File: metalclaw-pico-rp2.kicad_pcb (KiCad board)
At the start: 4 copper layers, 21 x 51 mm, 123 parts, among them J1 USB4105-GF-A, J2 FTSH-105-01-L-DV-K, SW1 PTS810SJM250SMTR LFS, SW2 PTS810SJM250SMTR LFS, U1 XC6220B331MR-G, U2 RP2354B, U3 APS6404L-3SQR-SN, Y1 ABM8-272-T3

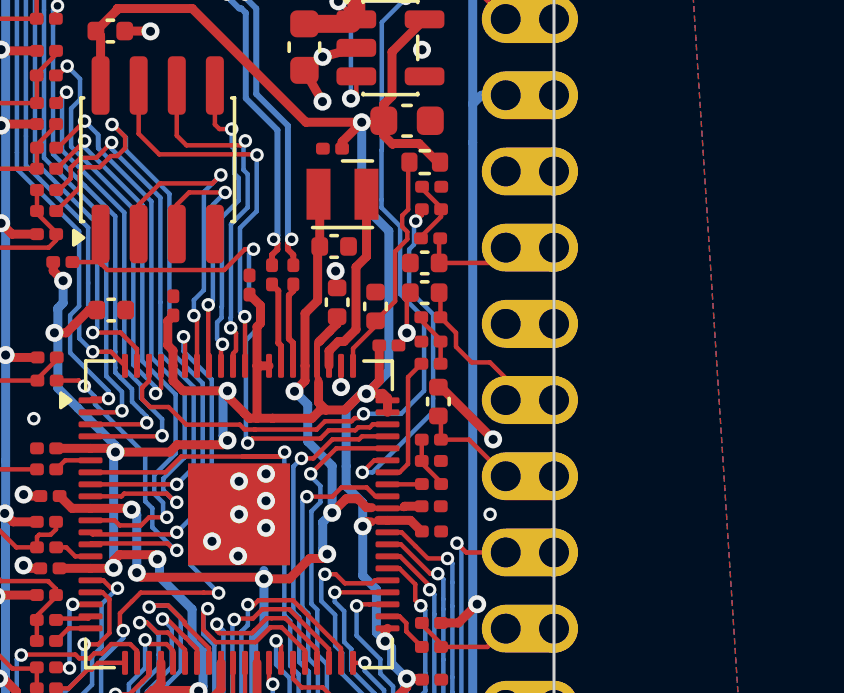
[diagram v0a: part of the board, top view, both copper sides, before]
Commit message: Add GND return vias for C29 and C9 decoupling loops
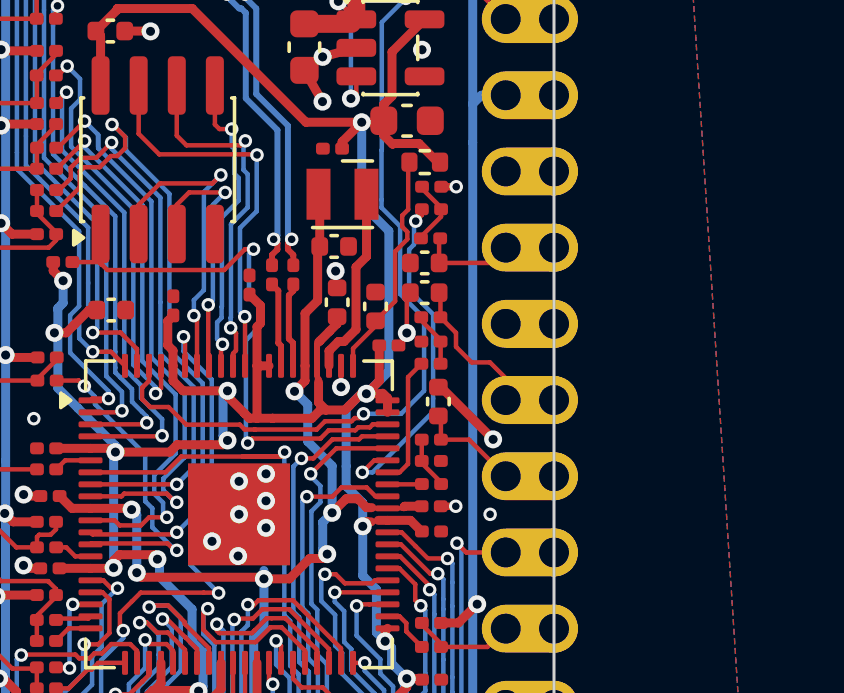
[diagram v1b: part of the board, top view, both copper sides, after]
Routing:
- net GND: track 23.9 -> 24.9 mm, vias 29 -> 31
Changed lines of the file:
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@@
 			(size 0.65 0.65)
 			(drill 0.65)
-			(layers "*.Cu" "*.Mask")
+			(layers "F&B.Cu" "*.Mask")
 		)
 		(pad "" np_thru_hole circle
@@
 			(size 0.65 0.65)
 			(drill 0.65)
-			(layers "*.Cu" "*.Mask")
+			(layers "F&B.Cu" "*.Mask")
 		)
 		(pad "A1" smd roundrect
@@
 	)
 	(segment
+		(start 170.535 98.6)
+		(end 171.035 98.6)
+		(width 0.25)
+		(layer "F.Cu")
+		(net 4)
+	)
+	(segment
 		(start 167.72 83.32)
 		(end 166.597111 83.620877)
@@
 	)
 	(segment
+		(start 170.55 87.95)
+		(end 171.05 87.95)
+		(width 0.25)
+		(layer "F.Cu")
+		(net 4)
+	)
+	(segment
 		(start 161.17 81.12)
 		(end 160.464874 81.308937)
@@
 	)
 	(via
+		(at 171.035 98.6)
+		(size 0.45)
+		(drill 0.25)
+		(layers "F.Cu" "B.Cu")
+		(net 4)
+	)
+	(via
 		(at 156.97 95.68)
 		(size 0.45)
@@
 		(layers "F.Cu" "B.Cu")
 		(net 4)
+	)
+	(via
+		(at 171.05 87.95)
+		(size 0.45)
+		(drill 0.25)
+		(layers "F.Cu" "B.Cu")
+		(net 4)

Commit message: Ground some passives better
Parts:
- moved R23 0.17 mm to (170.2, 89.5)
- moved C5 0.14 mm to (170.0, 91.3), turned to 180 degrees
- moved C4 0.07 mm to (170.0, 90.4), turned to 180 degrees
- turned R32 to 180 degrees
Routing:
- net Net-(A1-GPIO28_ADC2): track 3.32 -> 4.64 mm
- net Net-(A1-GPIO27_ADC1): track 4.92 -> 5.83 mm
- net Net-(C9-Pad2): track 2.54 -> 1.67 mm
- net GND: track 24.9 -> 24.2 mm

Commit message: Fix DRC warnings
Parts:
- moved R23 0.09 mm to (170.2, 89.4)
- moved C4 0.08 mm to (170.0, 90.3)
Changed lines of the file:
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@@
 	(footprint "Resistor_SMD:R_0201_0603Metric"
 		(layer "F.Cu")
-		(at 170.195 89.5)
+		(at 170.19 89.41)
 		(descr "Resistor SMD 0201 (0603 Metric), square (rectangular) end terminal, IPC-7351 nominal, (Body size source: https://www.vishay.com/docs/20052/crcw0201e3.pdf), generated with kicad-footprint-generator")
 		(tags "resistor")
@@
 	(footprint "Capacitor_SMD:C_0402_1005Metric"
 		(layer "F.Cu")
-		(at 170 90.42 180)
+		(at 170 90.34 180)
 		(descr "Capacitor SMD 0402 (1005 Metric), square (rectangular) end terminal, IPC-7351 nominal, (Body size source: IPC-SM-782 page 76, https://www.pcb-3d.com/wordpress/wp-content/uploads/ipc-sm-782a_amendment_1_and_2.pdf), generated with kicad-footprint-generator")
 		(tags "capacitor")
@@
 	)
 	(segment
-		(start 169.52 90.43)
-		(end 169.648518 90.43)
+		(start 172.2 89.48)
+		(end 172.7 89.98)
 		(width 0.15)
 		(layer "F.Cu")
@@
 	)
 	(segment
-		(start 169.52 90.42)
-		(end 169.648518 90.42)
+		(start 169.52 90.43)
+		(end 169.648518 90.43)
 		(width 0.15)
 		(layer "F.Cu")
@@
 	)
 	(segment
-		(start 172.22 89.5)
-		(end 172.7 89.98)
+		(start 169.52 90.42)
+		(end 169.648518 90.42)
 		(width 0.15)
 		(layer "F.Cu")
@@
 	)
 	(segment
-		(start 170.515 89.5)
-		(end 172.22 89.5)
+		(start 169.648518 90.34)
+		(end 169.52 90.34)
 		(width 0.15)
 		(layer "F.Cu")
@@
 	)
 	(segment
-		(start 170.515 89.553518)
-		(end 170.515 89.5)
+		(start 170.51 89.478518)
+		(end 169.648518 90.34)
 		(width 0.15)
 		(layer "F.Cu")
@@
 	)
 	(segment
-		(start 169.648518 90.42)
-		(end 170.515 89.553518)
+		(start 172.19 90.49)
+		(end 172.7 89.98)
 		(width 0.15)
 		(layer "F.Cu")
@@
 	)
 	(segment
-		(start 172.19 90.49)
-		(end 172.7 89.98)
+		(start 170.515 89.48)
+		(end 172.2 89.48)
 		(width 0.15)
 		(layer "F.Cu")
@@
 	)
 	(segment
-		(start 169.19 89.884)
-		(end 169.014 90.06)
-		(width 0.15)
-		(layer "F.Cu")
-		(net 15)
-	)
-	(segment
 		(start 169.35 88.561196)
 		(end 169.454 88.457196)
@@
 	)
 	(segment
-		(start 169.014 90.06)
-		(end 169.014 91.766)
+		(start 169.35 89.6)
+		(end 169.35 88.561196)
 		(width 0.15)
 		(layer "F.Cu")
@@
 	)
 	(segment
-		(start 169.35 89.724)
-		(end 169.35 88.561196)
+		(start 169.014 89.936)
+		(end 169.35 89.6)
 		(width 0.15)
 		(layer "F.Cu")
@@
 	)
 	(segment
-		(start 169.014 90.06)
-		(end 169.35 89.724)
+		(start 169.014 91.766)
+		(end 169.014 89.936)
 		(width 0.15)
 		(layer "F.Cu")

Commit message: Use net tie to connect AGND and GND
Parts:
- added NT1: NetTie_2, NetTie:NetTie-2_SMD_Pad0.5mm, B.Cu at (171.4, 91.7)
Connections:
- A1 pad 33: GND -> Net-(A1-AGND)
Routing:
- net Net-(A1-AGND): track 0.00 -> 1.45 mm
- net +3.3VP: track 143.4 -> 144.2 mm
- net GND: track 24.2 -> 24.8 mm, vias 31 -> 32
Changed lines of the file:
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@@
 	(net 115 "unconnected-(A1-ADC_VREF-Pad35)_1")
 	(net 116 "unconnected-(A1-VBUS-Pad40)_1")
+	(net 117 "Net-(A1-AGND)")
 	(footprint "Resistor_SMD:R_0201_0603Metric"
 		(layer "F.Cu")
@@
 			(remove_unused_layers no)
 			(roundrect_rratio 0.5)
-			(net 4 "GND")
+			(net 117 "Net-(A1-AGND)")
 			(pinfunction "AGND")
 			(pintype "power_out")
@@
 			(layers "*.Cu" "*.Mask")
 			(remove_unused_layers no)
-			(net 4 "GND")
+			(net 117 "Net-(A1-AGND)")
 			(pinfunction "AGND")
 			(pintype "power_out")
@@
 		)
 	)
+	(footprint "NetTie:NetTie-2_SMD_Pad0.5mm"
+		(layer "B.Cu")
+		(at 171.37 91.73 -90)
+		(descr "Net tie, 2 pin, 0.5mm square SMD pads")
+		(tags "net tie")
+		(property "Reference" "NT1"
+			(at 0 1.2 90)
+			(layer "B.SilkS")
+			(hide yes)
+			(effects
+				(font
+					(size 1 1)
+					(thickness 0.15)
+				)
+				(justify mirror)
+			)
+		)
+		(property "Value" "NetTie_2"
+			(at 0 -1.2 90)
+			(layer "B.Fab")
+			(hide yes)
+			(effects
+				(font
+					(size 1 1)
+					(thickness 0.15)
+				)
+				(justify mirror)
+			)
+		)
+		(property "Datasheet" "~"
+			(at 0 0 90)
+			(unlocked yes)
+			(layer "B.Fab")
+			(hide yes)
+			(effects
+				(font
+					(size 1.27 1.27)
+					(thickness 0.15)
+				)
+				(justify mirror)
+			)
+		)
+		(property "Description" "Net tie, 2 pins"
+			(at 0 0 90)
+			(unlocked yes)
+			(layer "B.Fab")
+			(hide yes)
+			(effects
+				(font
+					(size 1.27 1.27)
+					(thickness 0.15)
+				)
+				(justify mirror)
+			)
+		)
+		(property ki_fp_filters "Net*Tie*")
+		(sheetname "/")
+		(sheetfile "metalclaw-pico-rp2.kicad_sch")
+		(attr exclude_from_pos_files exclude_from_bom allow_missing_courtyard)
+		(net_tie_pad_groups "1, 2")
+		(fp_poly
+			(pts
+				(xy -0.5 0.25) (xy 0.5 0.25) (xy 0.5 -0.25) (xy -0.5 -0.25)
+			)
+			(stroke
+				(width 0)
+				(type solid)
+			)
+			(fill yes)
+			(layer "B.Cu")
+		)
+		(pad "1" smd circle
+			(at -0.5 0 270)
+			(size 0.5 0.5)
+			(layers "B.Cu")
+			(net 4 "GND")
+			(pinfunction "1")
+			(pintype "passive")
+		)
+		(pad "2" smd circle
+			(at 0.5 0 270)
+			(size 0.5 0.5)
+			(layers "B.Cu")
+			(net 117 "Net-(A1-AGND)")
+			(pinfunction "2")
+			(pintype "passive")
+		)
+		(embedded_fonts no)
+	)
 	(segment
 		(start 165.9 104.64)
@@
 	)
 	(via
+		(at 171.99 91.23)
+		(size 0.6)
+		(drill 0.3)
+		(layers "F.Cu" "B.Cu")
+		(net 4)
+	)
+	(via
 		(at 166.597111 83.620877)
 		(size 0.6)
@@
 	)
 	(segment
+		(start 171.37 91.23)
+		(end 171.99 91.23)
+		(width 0.6)
+		(layer "B.Cu")
+		(net 4)
+	)
+	(segment
 		(start 167.1 122.02)
 		(end 166.35 122.77)
@@
 	)
 	(segment
-		(start 171.599 120.839)
-		(end 171.599 121.189)
+		(start 170.656 96.886)
+		(end 170.656 90.024)
 		(width 0.3)
 		(layer "B.Cu")
@@
 	)
 	(segment
-		(start 171.599 121.189)
-		(end 172.12 121.71)
+		(start 156 98.84)
+		(end 156.03 98.81)
 		(width 0.3)
 		(layer "B.Cu")
@@
 	)
 	(segment
-		(start 156 98.84)
-		(end 156.03 98.81)
+		(start 171.599 89.081)
+		(end 171.599 85.19)
 		(width 0.3)
 		(layer "B.Cu")
@@
 	)
 	(segment
-		(start 156.026 100.33)
-		(end 156.026 121.504)
+		(start 172.12 121.71)
+		(end 171.599 121.189)
 		(width 0.3)
 		(layer "B.Cu")
@@
 	)
 	(segment
-		(start 172.7 84.9)
-		(end 171.889 84.9)
+		(start 156.026 100.33)
+		(end 156.026 121.504)
 		(width 0.3)
 		(layer "B.Cu")
@@
 	)
 	(segment
-		(start 171.599 86.48)
-		(end 171.599 85.19)
+		(start 172.7 84.9)
+		(end 171.889 84.9)
 		(width 0.3)
 		(layer "B.Cu")
@@
 	)
 	(segment
+		(start 171.599 121.189)
+		(end 171.599 97.829)
+		(width 0.3)
+		(layer "B.Cu")
+		(net 9)
+	)
+	(segment
 		(start 156.026 121.504)
 		(end 156.026 121.694)
@@
 	)
 	(segment
+		(start 170.656 90.024)
+		(end 171.599 89.081)
+		(width 0.3)
+		(layer "B.Cu")
+		(net 9)
+	)
+	(segment
 		(start 156.03 98.81)
 		(end 156.03 97.09)
@@
 	)
 	(segment
-		(start 171.599 86.48)
-		(end 171.599 120.839)
+		(start 171.599 97.829)
+		(end 170.656 96.886)
 		(width 0.3)
 		(layer "B.Cu")
@@
 	)
 	(segment
-		(start 168.26 97.47)
-		(end 170.28 95.45)
-		(width 0.15)
-		(layer "B.Cu")
-		(net 35)
-	)
-	(segment
-		(start 170.88 89.02)
-		(end 171.01 88.89)
+		(start 167.92 97.47)
+		(end 168.26 97.47)
 		(width 0.15)
 		(layer "B.Cu")
@@
 	)
 	(segment
-		(start 170.28 90.48)
-		(end 170.88 89.88)
+		(start 168.26 97.47)
+		(end 170.28 95.45)
 		(width 0.15)
 		(layer "B.Cu")
@@
 	(segment
 		(start 170.28 95.45)
-		(end 170.28 95.01)
-		(width 0.15)
-		(layer "B.Cu")
-		(net 35)
-	)
-	(segment
-		(start 170.28 92.2)
-		(end 170.28 90.48)
-		(width 0.15)
-		(layer "B.Cu")
-		(net 35)
-	)
-	(segment
-		(start 170.88 89.88)
-		(end 170.88 89.02)
+		(end 170.28 89.62)
 		(width 0.15)
 		(layer "B.Cu")
@@
 	)
 	(segment
-		(start 170.28 92.2)
-		(end 170.28 95.01)
-		(width 0.15)
-		(layer "B.Cu")
-		(net 35)
-	)
-	(segment
-		(start 167.92 97.47)
-		(end 168.26 97.47)
+		(start 170.28 89.62)
+		(end 171.01 88.89)
 		(width 0.15)
 		(layer "B.Cu")
@@
 		(net 114)
 	)
+	(segment
+		(start 171.66 92.52)
+		(end 171.37 92.23)
+		(width 0.6)
+		(layer "B.Cu")
+		(net 117)
+	)
+	(segment
+		(start 172.7 92.52)
+		(end 171.66 92.52)
+		(width 0.6)
+		(layer "B.Cu")
+		(net 117)
+	)
 	(zone

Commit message: Fix last warning and regen fab
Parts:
- J1: footprint Connector_USB:USB_C_Receptacle_GCT_USB4105-xx-A_16P_TopMnt_Horizontal -> MetalClaw:USB_C_Receptacle_GCT_USB4105-xx-A_16P_TopMnt_Horizontal
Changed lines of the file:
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@@
 		)
 	)
-	(footprint "Connector_USB:USB_C_Receptacle_GCT_USB4105-xx-A_16P_TopMnt_Horizontal"
+	(footprint "MetalClaw:USB_C_Receptacle_GCT_USB4105-xx-A_16P_TopMnt_Horizontal"
 		(locked yes)
 		(layer "F.Cu")

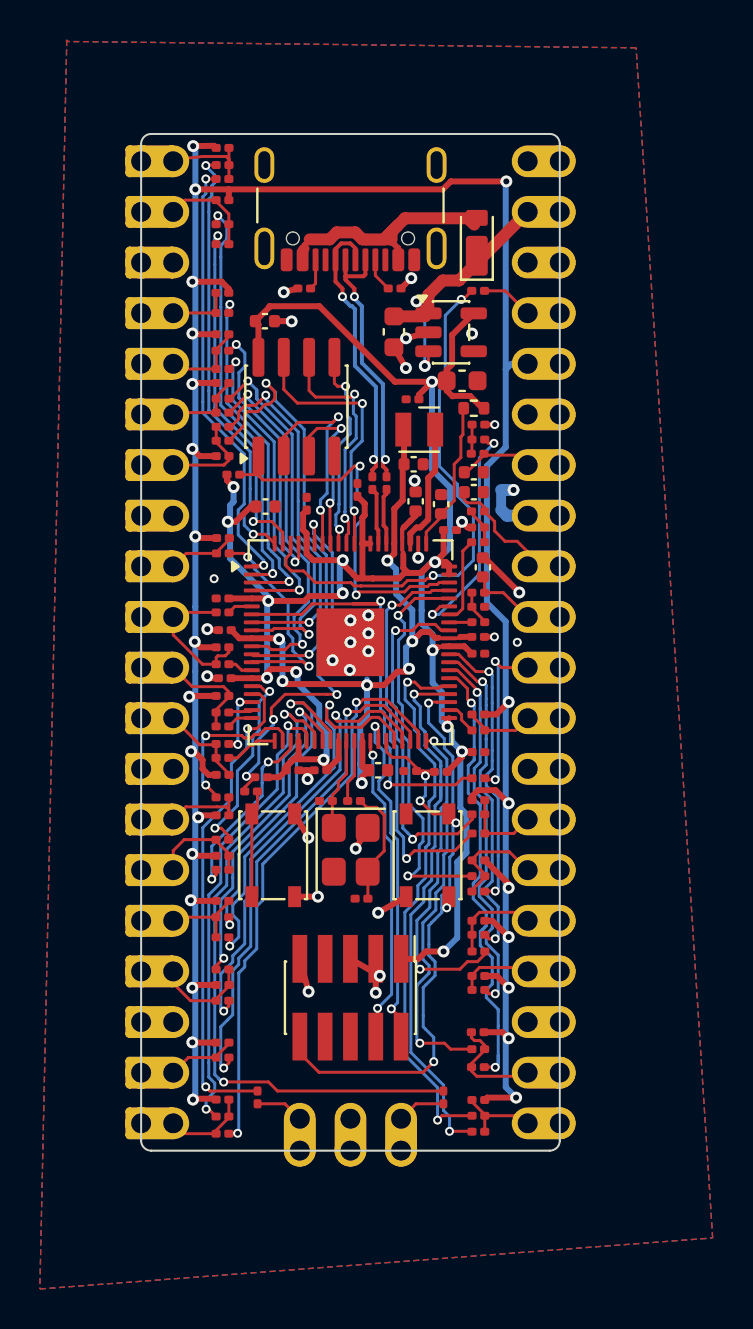
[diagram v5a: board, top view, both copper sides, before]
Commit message: Add test points for usb and debugger
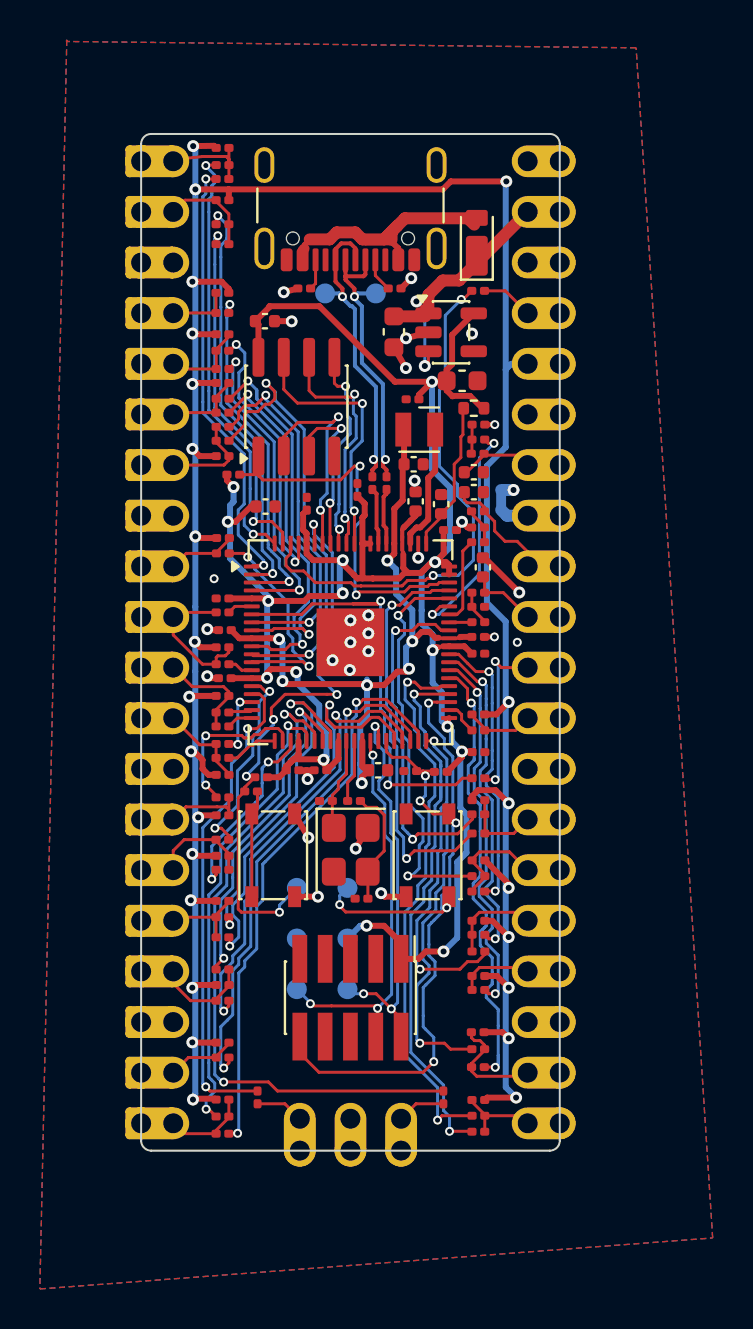
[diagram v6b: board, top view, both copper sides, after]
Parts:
- added TP1: TestPoint, TestPoint:TestPoint_Pad_D1.0mm, B.Cu at (165.1, 81.4)
- added TP2: TestPoint, TestPoint:TestPoint_Pad_D1.0mm, B.Cu at (162.5, 81.4)
- added TP3: TestPoint, TestPoint:TestPoint_Pad_D1.0mm, B.Cu at (161.1, 116.3)
- added TP4: TestPoint, TestPoint:TestPoint_Pad_D1.0mm, B.Cu at (163.7, 116.3)
- added TP5: TestPoint, TestPoint:TestPoint_Pad_D1.0mm, B.Cu at (163.7, 113.7)
- added TP6: TestPoint, TestPoint:TestPoint_Pad_D1.0mm, B.Cu at (161.1, 113.7)
- added TP7: TestPoint, TestPoint:TestPoint_Pad_D1.0mm, B.Cu at (163.7, 111.2)
- added TP8: TestPoint, TestPoint:TestPoint_Pad_D1.0mm, B.Cu at (161.1, 111.2)
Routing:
- net /BOOTSEL: track 19.6 -> 29.3 mm, vias 4 -> 5
- net /RESET: track 29.6 -> 36.2 mm, vias 5 -> 6
- net GND: track 24.8 -> 19.4 mm, vias 32 -> 29
- net Net-(J2-Pin_4): track 15.6 -> 20.1 mm, vias 2 -> 3
- net +3V3: track 119.2 -> 123.3 mm, vias 14 -> 15
- net Net-(J2-Pin_2): track 17.4 -> 20.0 mm, vias 2 -> 3
- net /USB_D-: track 13.6 -> 14.8 mm
- net /USB_D+: track 14.3 -> 15.2 mm

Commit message: Fix cap value
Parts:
- C11: value 1u -> 4.7u
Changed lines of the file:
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@@
 			)
 		)
-		(property "Value" "1u"
+		(property "Value" "4.7u"
 			(at 0 1.16 0)
 			(layer "F.Fab")
@@
 			)
 		)
-		(property "Datasheet" "https://eu.mouser.com/en/ProductDetail/TDK/C1005X7S1A105K050BC"
+		(property "Datasheet" "https://product.tdk.com/en/search/capacitor/ceramic/mlcc/info?part_no=C1005X5R0J475K050BC"
 			(at 0 0 0)
 			(layer "F.Fab")
@@
 			)
 		)
-		(property "Description" "1 uF +/-10% 10 V X7S 0402 carrier MCU decoupling capacitor, TDK C1005X7S1A105K050BC"
+		(property "Description" "4.7 uF 6.3 V X5R +/-10% 0402 regulator input capacitor (CIN), TDK C1005X5R0J475K050BC"
 			(at 0 0 0)
 			(layer "F.Fab")
@@
 			)
 		)
-		(property "Mouser" "810-C1005X7S1A105K"
+		(property "Mouser" "810-C1005X5R0J475K"
 			(at 0 0 180)
 			(unlocked yes)
@@
 			)
 		)
-		(property "LCSC" "C52923"
+		(property "LCSC" "C326586"
 			(at 0 0 270)
 			(unlocked yes)
@@
 			)
 		)
-		(property "LCSC MPN" "CL05A105KA5NQNC"
+		(property "LCSC MPN" "CC0402KRX5R6BB475"
 			(at 0 0 270)
 			(unlocked yes)

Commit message: Add silkscreen for product name and version
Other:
- board text added: "metalclaw pico-rp2 v1.r0"
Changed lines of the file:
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@@
 		(embedded_fonts no)
+	)
+	(gr_text "metalclaw\npico-rp2\nv1.r0"
+		(at 163.89 121.86 0)
+		(layer "B.SilkS")
+		(effects
+			(font
+				(size 1 1)
+				(thickness 0.15)
+			)
+			(justify bottom mirror)
+		)
 	)
 	(segment
